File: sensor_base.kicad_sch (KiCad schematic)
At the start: 40 parts, among them J14 Conn_01x02_Pin, J2 Conn_Coaxial, U1 MCP3204, U10 REF3040, U11 OPA2397DGKR, U2 TLV2387DR, U3 TPS22929D, U9 REF3025

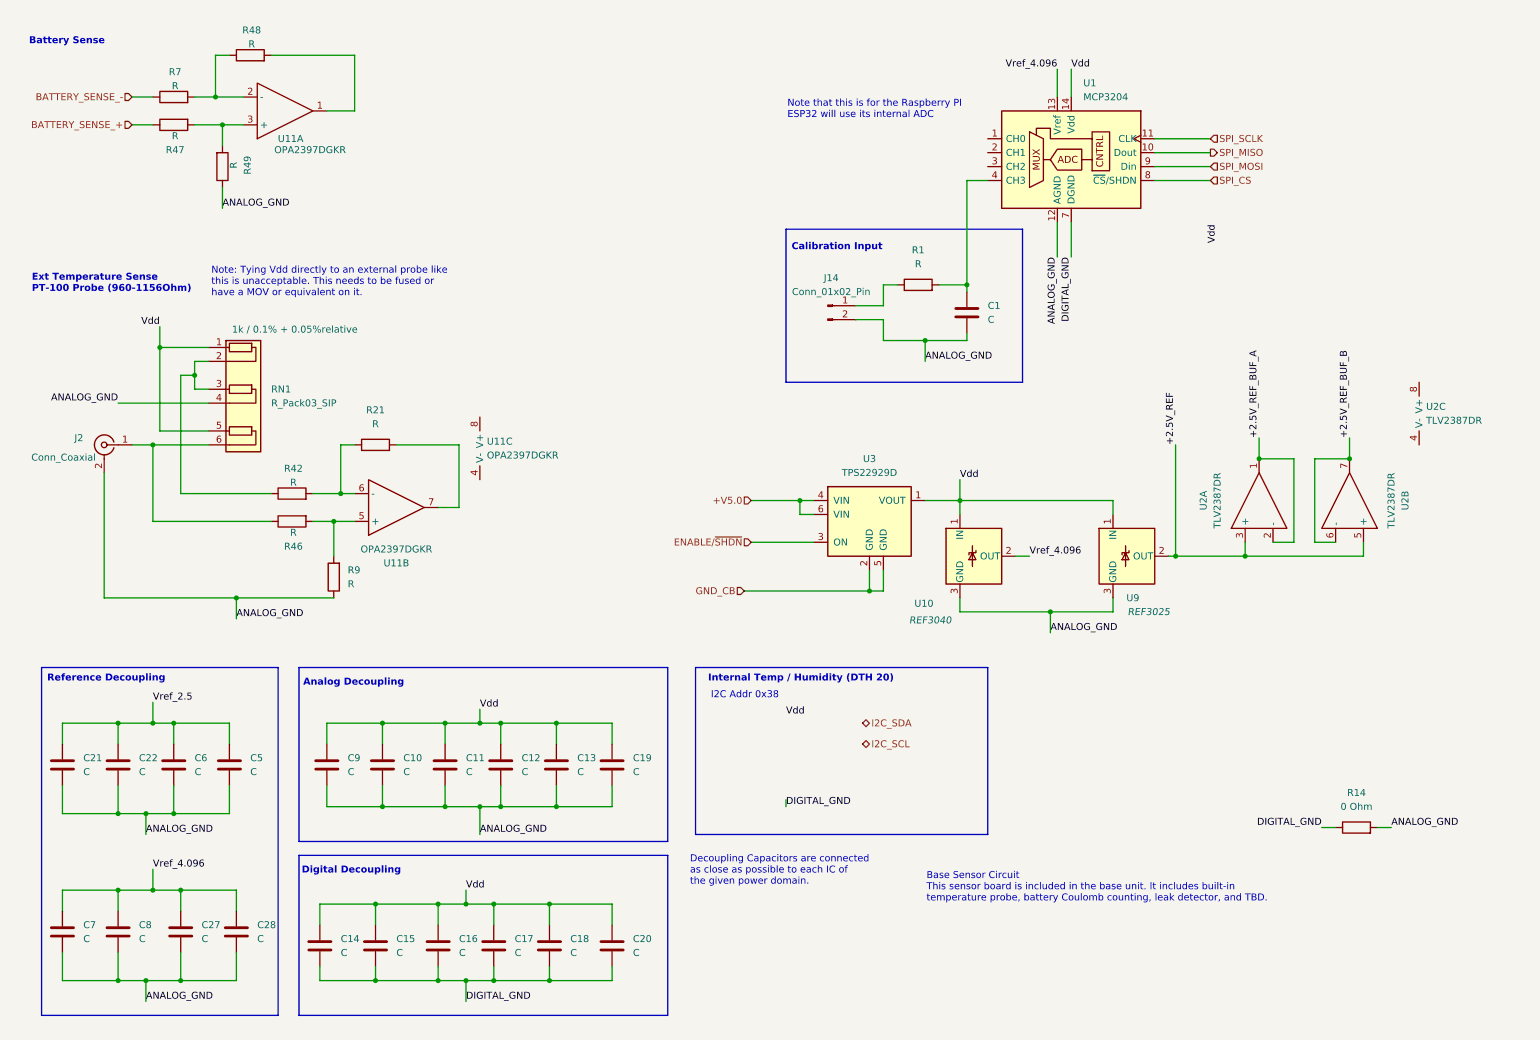
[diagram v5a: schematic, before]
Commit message: More notes and comments Cleaned up some signal lines Compacted the decoupling sections Added Turbidity placeholder
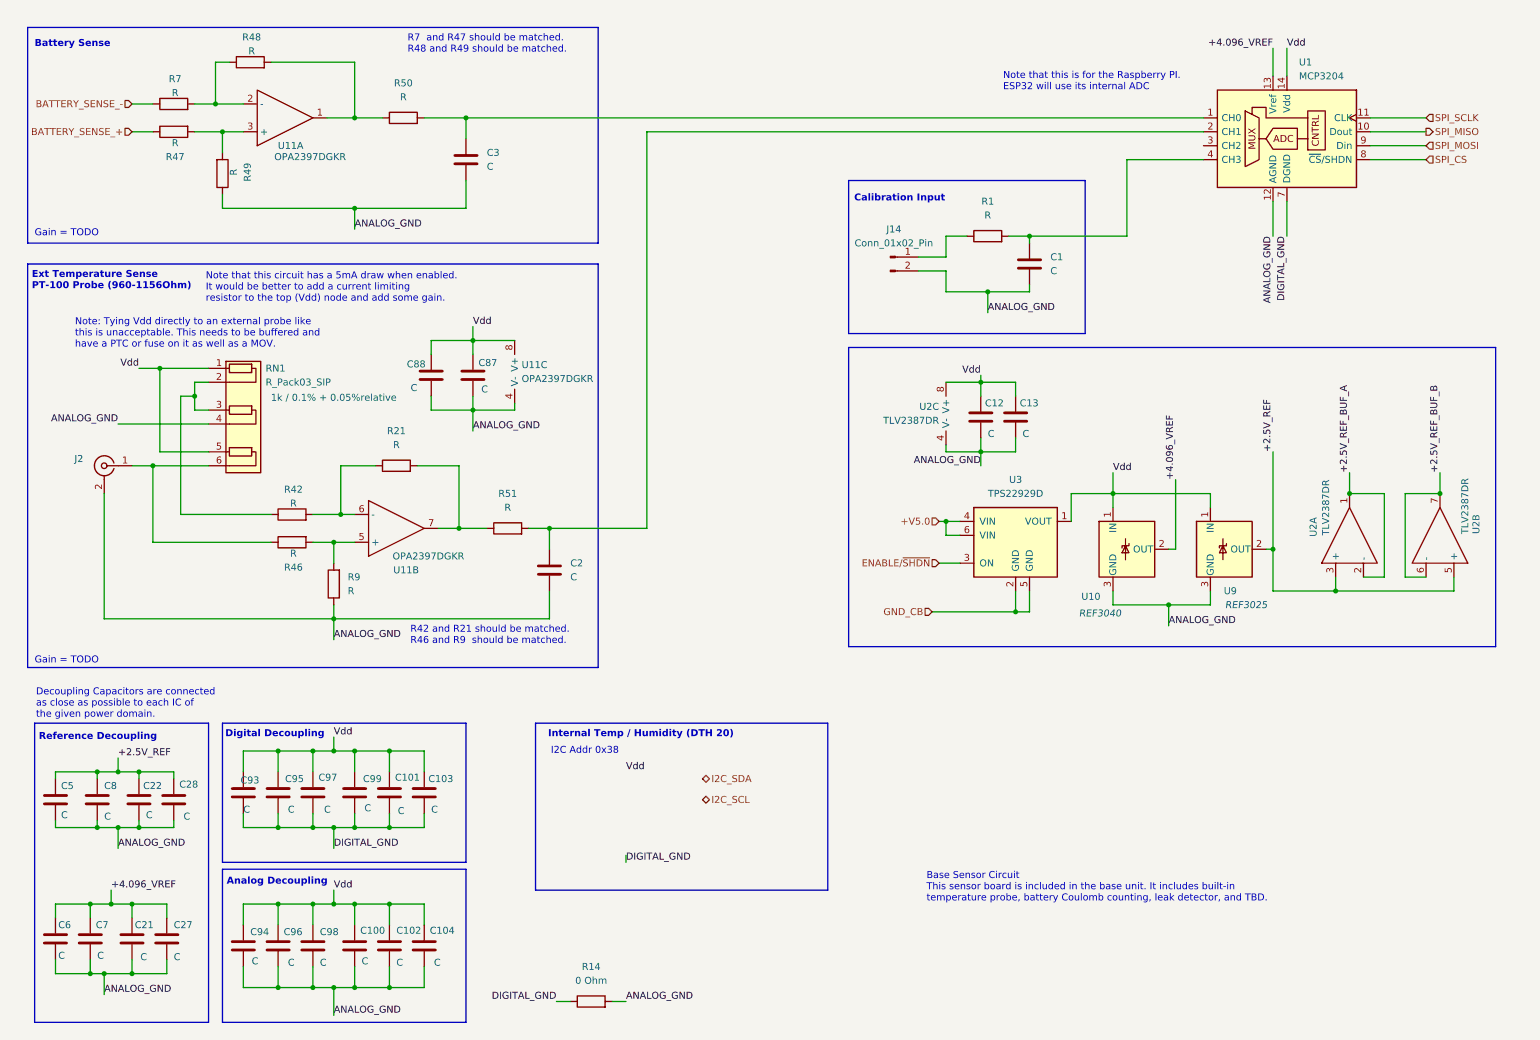
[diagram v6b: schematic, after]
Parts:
- removed C10, C11, C14, C15, C16, C17, C18, C19, C20, C9: C, symbol Device:C
- added C100, C101, C102, C103, C104, C2, C3, C87, C88, C93, C94, C95, C96, C97, C98, C99: C, symbol Device:C
- added R50, R51: R, symbol Device:R
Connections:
- net +2.5V_REF: now also C22.1, C28.1, C5.1, C8.1
- net ANALOG_GND: now also U11.4 (V-), U2.4 (V-), C100.2, C102.2, C104.2, C2.2, C3.2, C87.2, C88.2, C94.2, C96.2, C98.2
- net DIGITAL_GND: now also C101.2, C103.2, C93.2, C95.2, C97.2, C99.2
- net Vdd: now also U11.8 (V+), U2.8 (V+), C100.1, C101.1, C102.1, C103.1, C104.1, C87.1, C88.1, C93.1, C94.1, C95.1, C96.1, C97.1, C98.1, C99.1
- net at R48.2, U11.1: now also R50.1
- net at R21.2, U11.7: now also R51.1
- net at U1.1 (CH0): now also C3.1, R50.2
- net at U1.2 (CH1): now also C2.1, R51.2
- net Vref_2.5 renamed +4.096_VREF
- net +4.096_VREF: now also C27.1, C7.1, U1.13 (Vref), U10.2 (OUT); no longer C22.1, C5.1
- removed net Vref_4.096: C27.1, C28.1, C7.1, C8.1, U1.13 (Vref), U10.2 (OUT)
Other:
- note added: "Gain = TODO"
- note added: "Note that this circuit has a 5mA draw when enabled. It would be better to add a current limiting resistor to the top (Vdd) node and add some gain."
- note added: "Note that this is for the Raspberry PI. ESP32 will use its internal ADC"
- note added: "Note: Tying Vdd directly to an external probe like this is unacceptable. This needs to be buffered and have a PTC or fuse on it as well as a MOV."
- note added: "R42 and R21 should be matched. R46 and R9 should be matched."
- note added: "R7 and R47 should be matched. R48 and R49 should be matched."
- note removed: "Note that this is for the Raspberry PI ESP32 will use its internal ADC"
- note removed: "Note: Tying Vdd directly to an external probe like this is unacceptable. This needs to be fused or have a MOV or equivalent on it."
- moved on the sheet: C1, J14, J2, R1, R14, R21, R42, R46, R47, R48, R49, R7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

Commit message: Cleaned up a bit Added a SPDT to calibrate signal on the base board Added PTC and MOV to power section
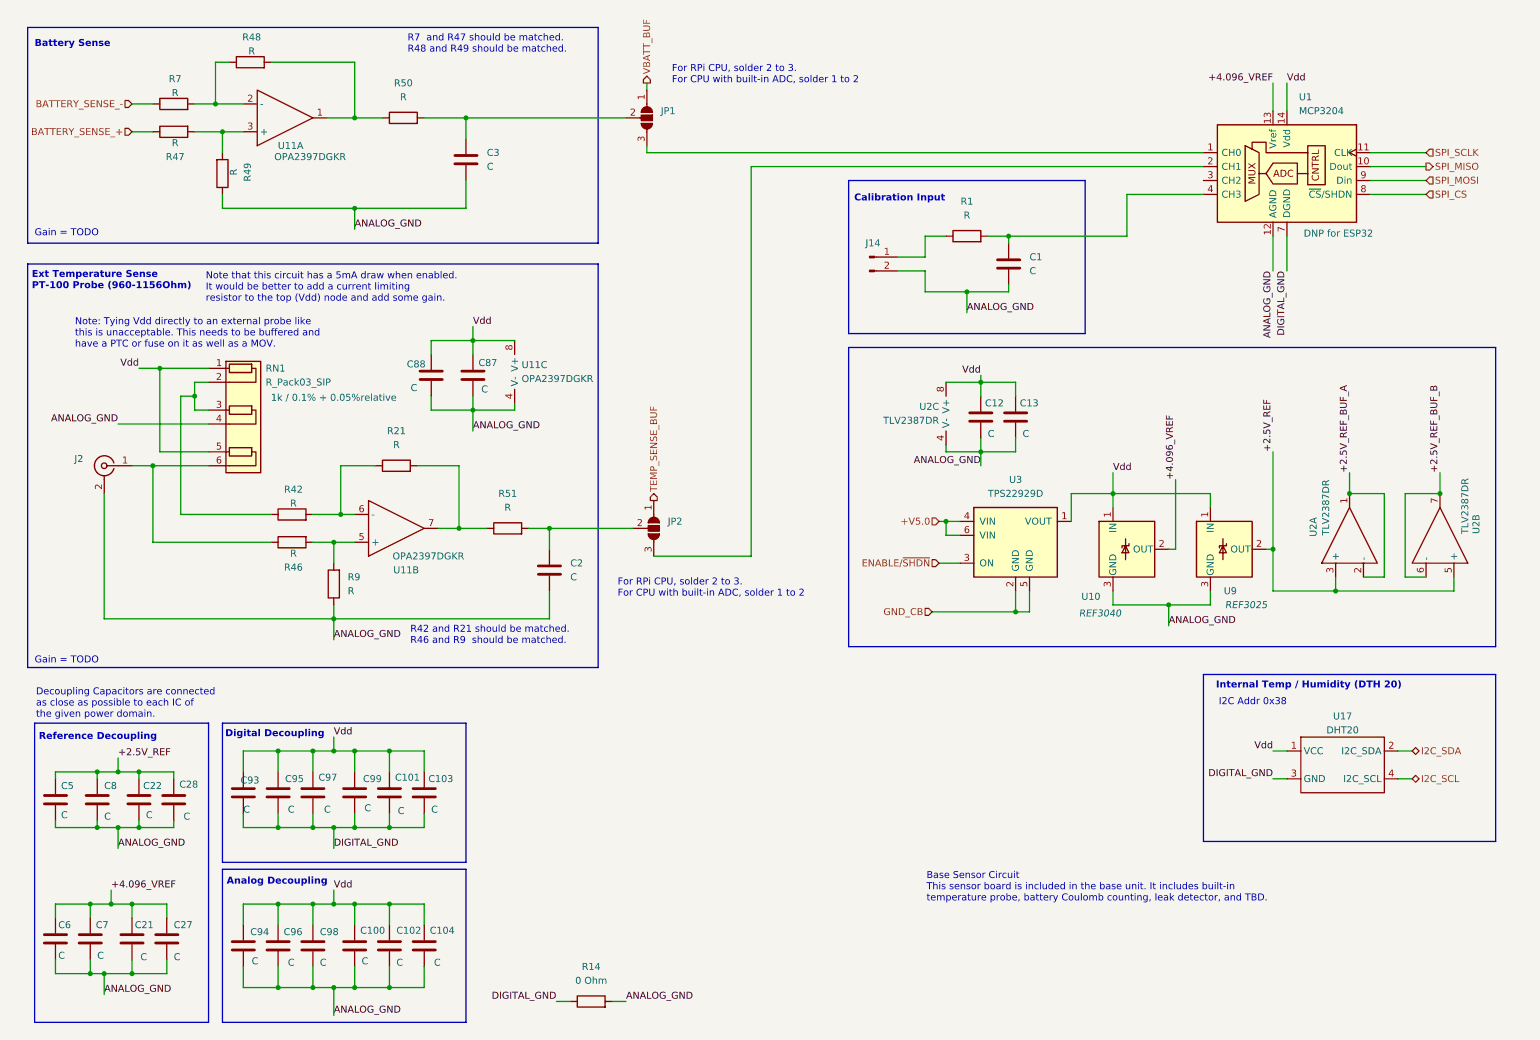
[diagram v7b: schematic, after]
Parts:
- added JP1, JP2: SolderJumper_3_Open, symbol Jumper:SolderJumper_3_Open
- added U17: DHT20, Connector_PinHeader_1.27mm:PinHeader_1x04_P1.27mm_Vertical, symbol AndrewAdditions:DHT20
- U1: NOTE (none) -> DNP for ESP32
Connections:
- net DIGITAL_GND: now also U17.3 (GND)
- net I2C_SCL: now also U17.4 (I2C_SCL)
- net I2C_SDA: now also U17.2 (I2C_SDA)
- net Vdd: now also U17.1 (VCC)
- net at C2.1, R51.2: now also JP2.2 (C); no longer U1.2 (CH1)
- net at C3.1, R50.2: now also JP1.2 (C); no longer U1.1 (CH0)
- new net: JP1.3 (B), U1.1 (CH0)
- new net: JP2.3 (B), U1.2 (CH1)
- new net TEMP_SENSE_BUF: JP2.1 (A)
- new net VBATT_BUF: JP1.1 (A)
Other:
- note added: "For RPi CPU, solder 2 to 3. For CPU with built-in ADC, solder 1 to 2"
- note removed: "Note that this is for the Raspberry PI. ESP32 will use its internal ADC"
- moved on the sheet: C1, J14, R1, U1

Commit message: Began assigning footprints Cleaned up some of the signalling and added the full prototype sensor suite Added a header for the Atlas Scientific carrier board Added some test points and jumpers Cleaned up the power section Started work on the CPU signal assignment and header sockets
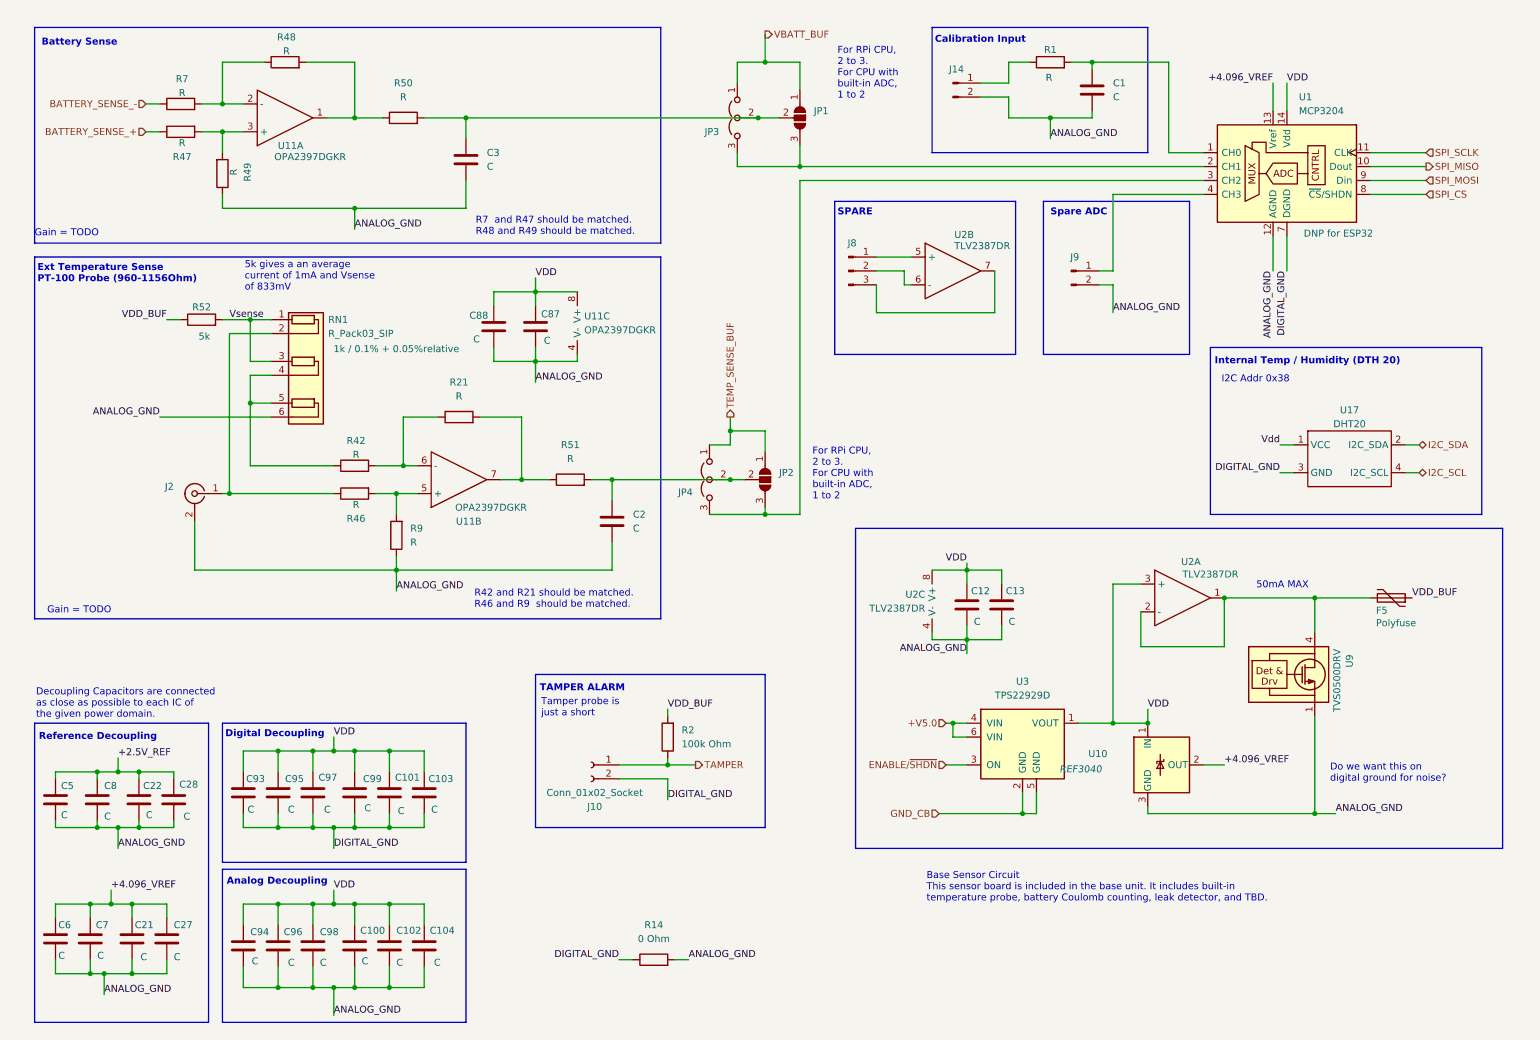
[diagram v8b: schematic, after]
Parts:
- removed U9: REF3025, Package_TO_SOT_SMD:SOT-23, symbol Reference_Voltage:REF3025
- added F5: Polyfuse, symbol Device:Polyfuse
- added J10: Conn_01x02_Socket, symbol Connector:Conn_01x02_Socket
- added J8: Conn_01x03_Pin, symbol Connector:Conn_01x03_Pin
- added J9: Conn_01x02_Pin, symbol Connector:Conn_01x02_Pin
- added JP3, JP4: Jumper_3_Open, symbol Jumper:Jumper_3_Open
- added R2: 100k Ohm, symbol Device:R
- added R52: 5k, symbol Device:R
- added U9: TVS0500DRV, Package_SON:WSON-6-1EP_2x2mm_P0.65mm_EP1x1.6mm, symbol Power_Protection:TVS0500DRV
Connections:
- net +2.5V_REF: no longer U2.3 (+), U2.5 (+)
- net ANALOG_GND: now also RN1.6 (R3.2), J9.2 (Pin_2), U9.1 (GND), U9.2 (GND), U9.3 (GND), U9.7 (GND); no longer RN1.4 (R2.2)
- net DIGITAL_GND: now also J10.2 (Pin_2)
- net TEMP_SENSE_BUF: now also JP4.1 (A)
- net VBATT_BUF: now also JP3.1 (A)
- net Vdd: no longer C100.1, C101.1, C102.1, C103.1, C104.1, C12.1, C13.1, C87.1, C88.1, C93.1, C94.1, C95.1, C96.1, C97.1, C98.1, C99.1, RN1.1 (R1.1), RN1.5 (R3.1), U1.14 (Vdd), U10.1 (IN), U11.8 (V+), U2.8 (V+), U3.1 (VOUT)
- net at C2.1, JP2.2 (C), R51.2: now also JP4.2 (C)
- net at C3.1, JP1.2 (C), R50.2: now also JP3.2 (C)
- net at J2.1 (In), R46.1: now also RN1.2 (R1.2); no longer RN1.6 (R3.2)
- net at JP1.3 (B): now also U1.2 (CH1), JP3.3 (B); no longer U1.1 (CH0)
- net at C1.1, R1.2: now also U1.1 (CH0); no longer U1.4 (CH3)
- net at JP2.3 (B): now also U1.3 (CH2), JP4.3 (B); no longer U1.2 (CH1)
- net +2.5V_REF_BUF_A: no longer names the net of U2.1, U2.2 (-)
- net +2.5V_REF_BUF_A: now also F5.2, U9.4 (IN), U9.5 (IN), U9.6 (IN)
- net +2.5V_REF_BUF_B: no longer names the net of U2.6 (-)
- net +2.5V_REF_BUF_B: now also J8.2 (Pin_2); no longer U2.7
- new net: J9.1 (Pin_1), U1.4 (CH3)
- new net: R42.1, RN1.4 (R2.2), RN1.5 (R3.1)
- new net: J8.1 (Pin_1), U2.5 (+)
- new net: J8.3 (Pin_3), U2.7
- new net TAMPER: J10.1 (Pin_1), R2.1
- new net VDD: C100.1, C101.1, C102.1, C103.1, C104.1, C12.1, C13.1, C87.1, C88.1, C93.1, C94.1, C95.1, C96.1, C97.1, C98.1, C99.1, U1.14 (Vdd), U10.1 (IN), U11.8 (V+), U2.3 (+), U2.8 (V+), U3.1 (VOUT)
- new net VDD_BUF: F5.1, R2.2, R52.1
- new net Vsense: R52.2, RN1.1 (R1.1), RN1.3 (R2.1)
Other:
- note added: "50mA MAX"
- note added: "5k gives a an average current of 1mA and Vsense of 833mV"
- note added: "Do we want this on digital ground for noise?"
- note added: "For RPi CPU, 2 to 3. For CPU with built-in ADC, 1 to 2"
- note added: "SPARE"
- note added: "Spare ADC"
- note added: "TAMPER ALARM"
- note added: "Tamper probe is just a short"
- note removed: "For RPi CPU, solder 2 to 3. For CPU with built-in ADC, solder 1 to 2"
- note removed: "Note that this circuit has a 5mA draw when enabled. It would be better to add a current limiting resistor to the top (Vdd) node and add some gain."
- note removed: "Note: Tying Vdd directly to an external probe like this is unacceptable. This needs to be buffered and have a PTC or fuse on it as well as a MOV."
- moved on the sheet: C1, C12, C13, C2, C87, C88, J14, J2, JP1, JP2, R1, R14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
